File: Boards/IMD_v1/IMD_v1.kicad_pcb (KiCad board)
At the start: 2 copper layers, 25 x 50 mm, 29 parts, among them J1 MM_F_RA_04, J2 UF_2_RA, K1 G5Q-1A4-DC5-5V, Q1 SSM3K333R, Q2 SSM3K333R, U1 Ultrafit_5(IMD), U2 TLV3701QDBVRG4Q1, U3 TLV3701QDBVRG4Q1, U4 CD4044BPWR

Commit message: Layout after check in with Corey
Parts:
- C1: footprint Formula:C_0805_OEM -> footprints:C_0805_OEM
- C2: footprint Formula:C_1206_OEM -> footprints:C_1206_OEM
- D1: footprint Formula:DO-214AA -> footprints:DO-214AA
- D2, D4: footprint Formula:LED_0805_OEM -> footprints:LED_0805_OEM
- D3: footprint Formula:D_0805_OEM -> footprints:D_0805_OEM
- F1: footprint Formula:Fuse_1210 -> footprints:Fuse_1210
- J1: footprint Formula:micromatch_female_ra_4 -> footprints:micromatch_female_ra_4
- J2: value UF_2_RA -> UF_2_VT; footprint Formula:Ultrafit_2_RA -> footprints:Ultrafit_2
- K1: footprint Formula:Relay_SPST_OMRON-G5Q-1A4_OEM -> footprints:Relay_SPST_OMRON-G5Q-1A4_OEM
- Q1, Q2: footprint Formula:SOT-23F -> footprints:SOT-23F
- R1, R10, R11, R12, R13, R2, R3, R4, R5, R6, R7, R8, R9: footprint Formula:R_0805_OEM -> footprints:R_0805_OEM
- U1: footprint Formula:Ultrafit_5 -> footprints:Ultrafit_5
- U2, U3: footprint Formula:SOT-23-5_OEM -> footprints:SOT-23-5_OEM
- U4: footprint Formula:TSSOP-16-OEM -> footprints:TSSOP-16-OEM
- moved J1 9.98 mm to (95.5, 89.2)
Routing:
- net +12V: track 11.0 -> 25.5 mm, vias 0 -> 2
- net GND: track 55.8 -> 68.7 mm, vias 6 -> 10
- net /IMD_Status_Output: track 63.6 -> 72.9 mm
- net /12V_Fused: track 90.6 -> 96.6 mm, vias 5 -> 6
- net (no net): track 5.06 -> 0.18 mm
- net Net-(D3-Pad2): track 33.8 -> 36.6 mm
- net Net-(J2-Pad2): track 17.5 -> 18.7 mm
- net Net-(D4-Pad1): track 23.6 -> 24.4 mm, vias 1 -> 0
- removed copper zone on F.Cu, net GND
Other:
- board text added: "GREEN = GOOD"
- board text removed: "LED ON = IMD GOOD"

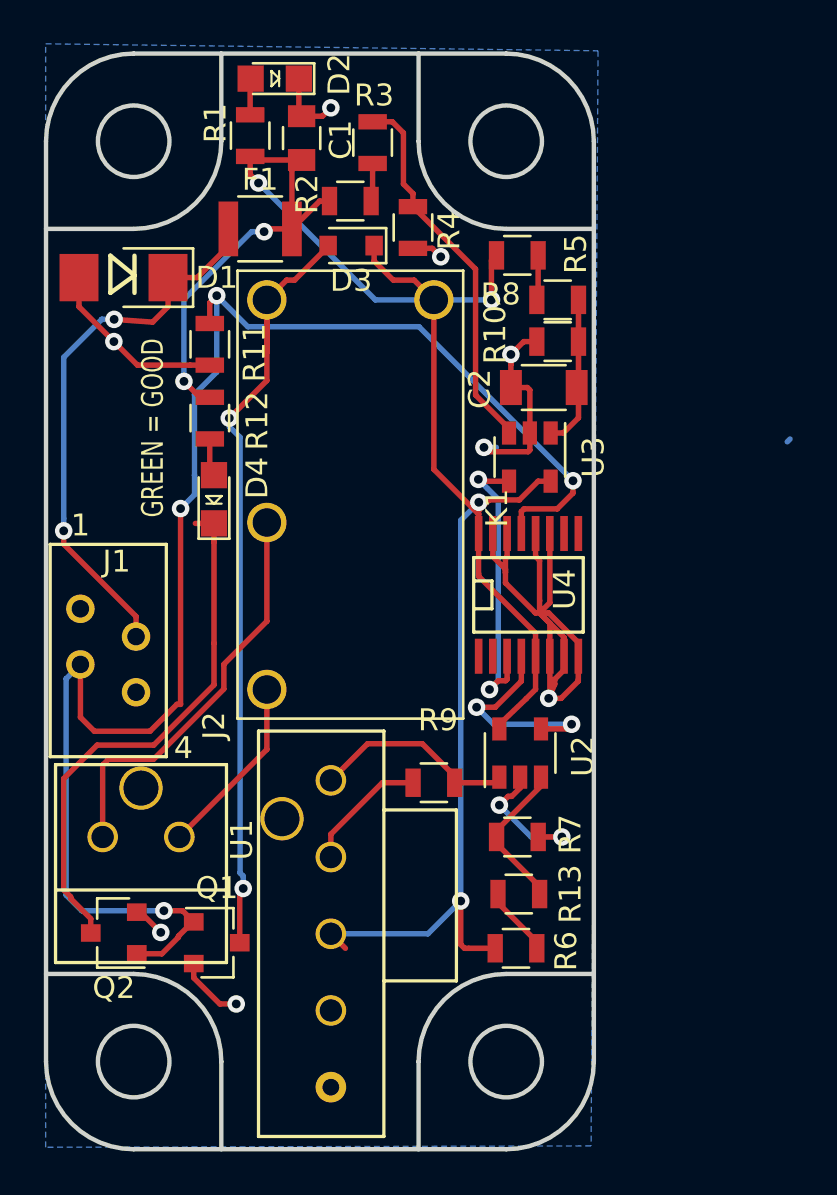
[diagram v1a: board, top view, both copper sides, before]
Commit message: Layout try 3, much less GND islands, and better silkscreen
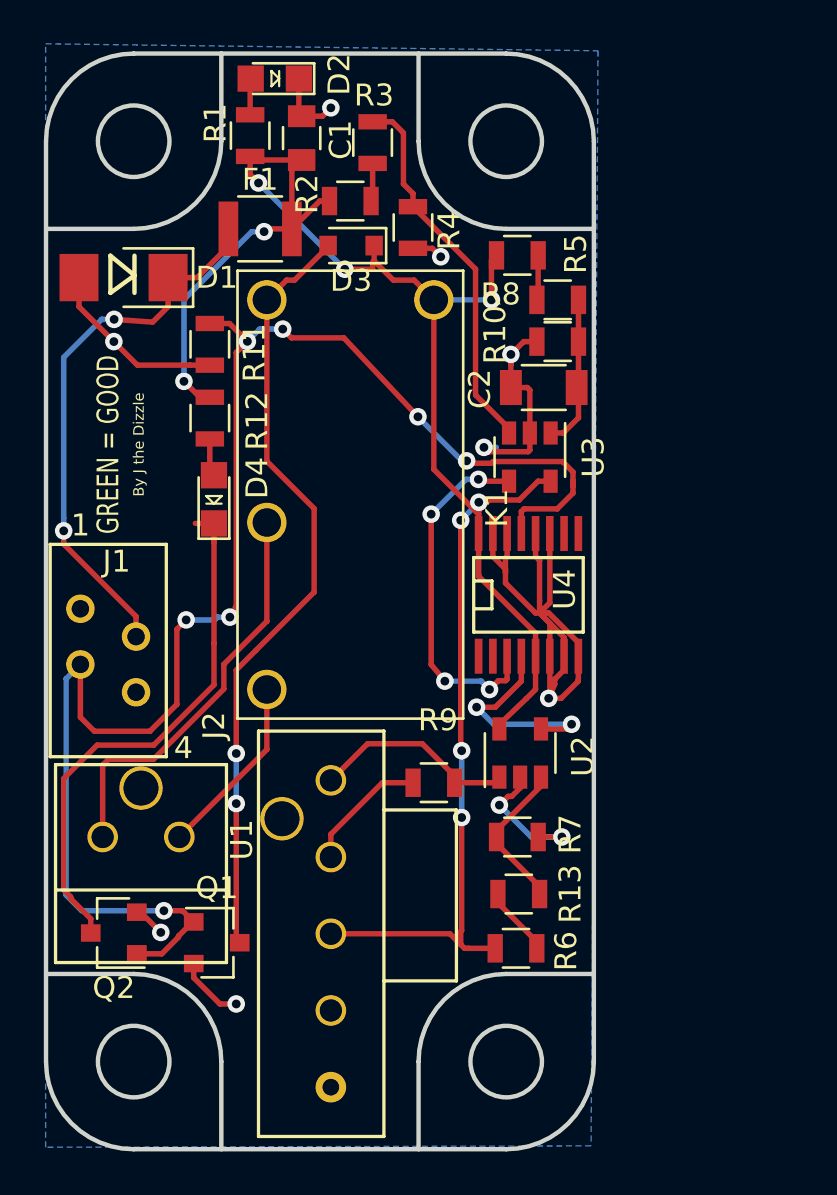
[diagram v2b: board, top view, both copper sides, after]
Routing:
- net /12V_Fused: track 96.6 -> 92.0 mm, vias 6 -> 9
- net Net-(U3-Pad4): track 13.6 -> 16.5 mm, vias 2 -> 4
- net Net-(D3-Pad2): track 36.6 -> 35.6 mm
- net /IMD_Status_Output: track 72.9 -> 72.8 mm, vias 4 -> 7
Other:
- net class formula added: clearance 0.1524, trace_width 0.1524, via_dia 0.6096, via_drill 0.3048
- rule trace_min: 0.2 -> 0.1524
- board text added: "By J the Dizzle"

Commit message: IMD Latch Comparator Fix
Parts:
- turned U2 to 270 degrees
- turned U3 to 90 degrees
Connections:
- U2 pad 3: Net-(R13-Pad2) -> /imd_side_out
- U2 pad 4: Net-(U2-Pad4) -> Net-(R13-Pad2)
- U3 pad 1: Net-(C2-Pad1) -> /delay_side_out
- U3 pad 3: Net-(R3-Pad2) -> Net-(C2-Pad1)
- U3 pad 4: Net-(U3-Pad4) -> Net-(R3-Pad2)
- U4 pad 3: Net-(U3-Pad4) -> /delay_side_out
- U4 pad 4: Net-(U2-Pad4) -> /imd_side_out
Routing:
- net Net-(U3-Pad4): track 16.5 -> 0.00 mm, vias 4 -> 0
- net /delay_side_out: track 0.00 -> 16.5 mm, vias 0 -> 4
- net Net-(U2-Pad4): track 9.81 -> 0.00 mm, vias 2 -> 0
- net Net-(R9-Pad1): track 9.40 -> 16.4 mm, vias 0 -> 2
- net /IMD_Status_Output: track 72.8 -> 68.4 mm
- net /imd_side_out: track 0.00 -> 3.94 mm
- net Net-(R3-Pad2): track 17.3 -> 20.1 mm, vias 0 -> 2
- net GND: track 68.7 -> 66.1 mm, vias 10 -> 8
- net Net-(C2-Pad1): track 6.94 -> 8.80 mm
- net /12V_Fused: track 92.0 -> 93.0 mm
- net Net-(R13-Pad2): track 6.99 -> 6.02 mm
- net Net-(J2-Pad2): track 18.7 -> 19.6 mm
- net Net-(D4-Pad1): vias 0 -> 2
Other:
- outline, holes or cut-outs redrawn
- net class Default: clearance 0.2 -> 0.1524; trace_width 0.25 -> 0.1524; via_dia 0.8 -> 0.6096; via_drill 0.4 -> 0.3048
- net class formula removed
- rule trace_clearance: 0.2 -> 0.1524
- rule via_min_drill: 0.3 -> 0.3048
- rule via_min_size: 0.4 -> 0.6096
- board text added: "IMD LATCH Jamie Santiago"
- board text removed: "By J the Dizzle"

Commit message: IMD update
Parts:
- J2: value UF_2_VT -> mm_2; footprint footprints:Ultrafit_2 -> footprints:mm_2
- moved J2 1.91 mm to (98.4, 94.5), turned to 180 degrees
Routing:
- net Net-(J2-Pad2): track 19.6 -> 15.5 mm
- net Net-(J2-Pad1): track 8.38 -> 10.6 mm

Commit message: IMD DRC checked
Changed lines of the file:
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@@
     (thickness 1.6)
     (drawings 26)
-    (tracks 338)
+    (tracks 335)
     (zones 0)
     (modules 29)
@@
   )
   (setup
-    (last_trace_width 0.762)
+    (last_trace_width 0.1524)
     (user_trace_width 0.762)
     (trace_clearance 0.1524)
@@
   (segment (start 104.013 84.6455) (end 104.013 80.137) (width 0.762) (layer F.Cu) (net 10))
   (segment (start 101.724598 88.648402) (end 100.05259 90.32041) (width 0.762) (layer F.Cu) (net 10))
-  (segment (start 101.724598 86.933902) (end 101.95759 86.70091) (width 0.762) (layer F.Cu) (net 10))
   (segment (start 101.724598 88.648402) (end 101.724598 86.933902) (width 0.762) (layer F.Cu) (net 10))
-  (segment (start 102.05001 86.60849) (end 101.95759 86.70091) (width 0.762) (layer F.Cu) (net 10))
-  (segment (start 101.95759 86.70091) (end 104.013 84.6455) (width 0.762) (layer F.Cu) (net 10))
   (segment (start 100.05259 91.59041) (end 98.425 93.218) (width 0.762) (layer F.Cu) (net 10))
   (segment (start 100.05259 90.32041) (end 100.05259 91.59041) (width 0.762) (layer F.Cu) (net 10))
+  (segment (start 104.013 84.6455) (end 101.724598 86.933902) (width 0.762) (layer F.Cu) (net 10))
   (segment (start 99.186999 94.996001) (end 98.425 95.758) (width 0.762) (layer F.Cu) (net 11))
   (segment (start 102.152401 92.030599) (end 99.186999 94.996001) (width 0.762) (layer F.Cu) (net 11))
@@
   (segment (start 115.626 86.239) (end 115.626 87.23433) (width 0.25) (layer F.Cu) (net 22))
   (via (at 113.665 78.1685) (size 0.8) (drill 0.4) (layers F.Cu B.Cu) (net 23))
-  (via (at 114.173 87.757) (size 0.8) (drill 0.4) (layers F.Cu B.Cu) (net 23))
-  (segment (start 114.976 87.289) (end 114.907999 87.357001) (width 0.25) (layer F.Cu) (net 23))
-  (segment (start 114.572999 87.357001) (end 114.173 87.757) (width 0.25) (layer F.Cu) (net 23))
-  (segment (start 114.907999 87.357001) (end 114.572999 87.357001) (width 0.25) (layer F.Cu) (net 23))
-  (segment (start 114.976 86.239) (end 114.976 87.289) (width 0.25) (layer F.Cu) (net 23))
   (segment (start 113.099315 78.1685) (end 111.511815 79.756) (width 0.25) (layer B.Cu) (net 23))
   (segment (start 113.665 78.1685) (end 113.099315 78.1685) (width 0.25) (layer B.Cu) (net 23))
   (via (at 111.511815 79.756) (size 0.8) (drill 0.4) (layers F.Cu B.Cu) (net 23))
   (segment (start 111.511815 79.756) (end 111.511815 86.619815) (width 0.25) (layer F.Cu) (net 23))
-  (via (at 112.134826 87.376) (size 0.8) (drill 0.4) (layers F.Cu B.Cu) (net 23))
   (segment (start 112.268 87.376) (end 112.134826 87.376) (width 0.25) (layer F.Cu) (net 23))
   (segment (start 111.511815 86.619815) (end 112.134826 87.376) (width 0.25) (layer F.Cu) (net 23))
-  (segment (start 113.792 87.376) (end 114.173 87.757) (width 0.25) (layer B.Cu) (net 23))
-  (segment (start 112.134826 87.376) (end 113.792 87.376) (width 0.25) (layer B.Cu) (net 23))
   (segment (start 113.749 78.2525) (end 113.665 78.1685) (width 0.1524) (layer F.Cu) (net 23))
   (segment (start 115.0645 78.2525) (end 113.749 78.2525) (width 0.25) (layer F.Cu) (net 23))
+  (segment (start 114.976 87.289) (end 114.641 87.289) (width 0.25) (layer F.Cu) (net 23))
+  (via (at 114.173 87.757) (size 0.8) (drill 0.4) (layers F.Cu B.Cu) (net 23))
+  (segment (start 114.641 87.289) (end 114.173 87.757) (width 0.25) (layer F.Cu) (net 23))
+  (segment (start 112.134826 87.376) (end 113.792 87.376) (width 0.25) (layer B.Cu) (net 23))
+  (segment (start 113.792 87.376) (end 114.173 87.757) (width 0.25) (layer B.Cu) (net 23))
+  (via (at 112.134826 87.376) (size 0.8) (drill 0.4) (layers F.Cu B.Cu) (net 23))
+  (segment (start 114.976 86.239) (end 114.976 87.289) (width 0.25) (layer F.Cu) (net 23))
   (zone (net 2) (net_name GND) (layer B.Cu) (hatch edge 0.508)
     (connect_pads (clearance 0.508))

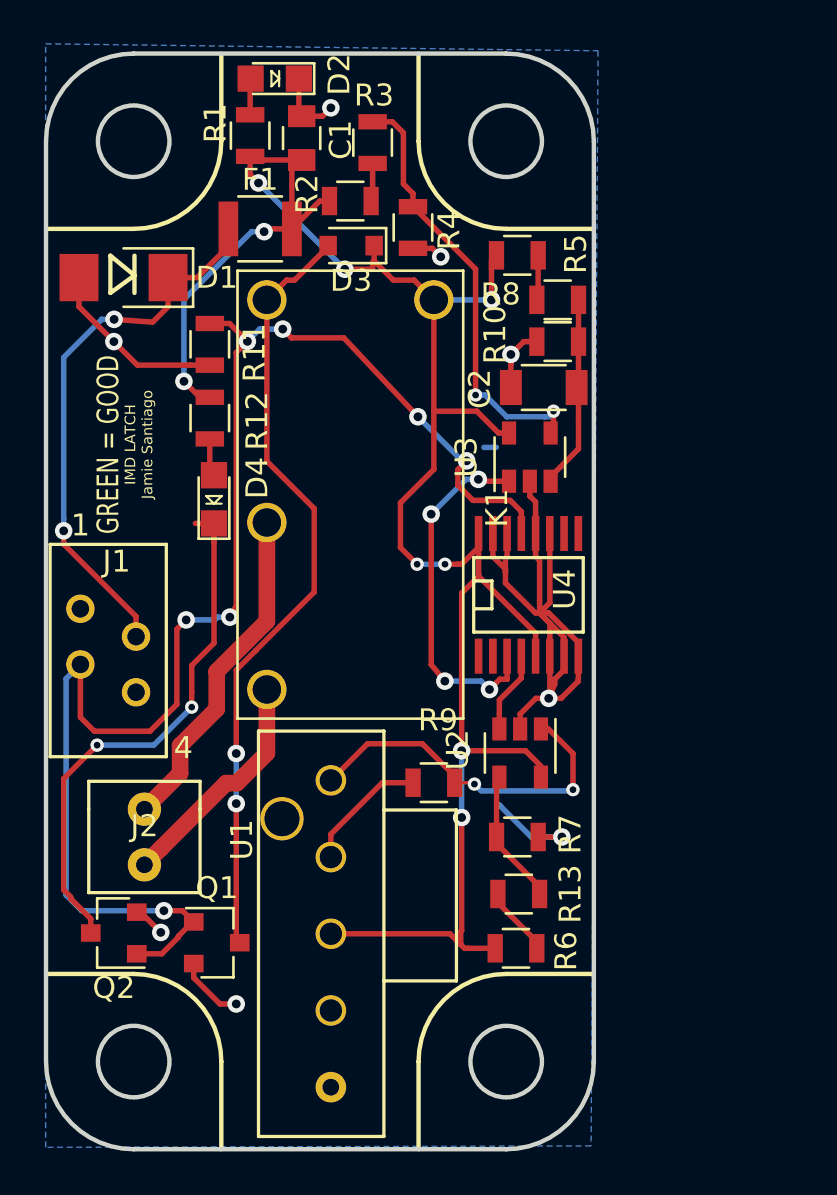
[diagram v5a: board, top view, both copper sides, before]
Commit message: Layout and Schematic with microfit v 2
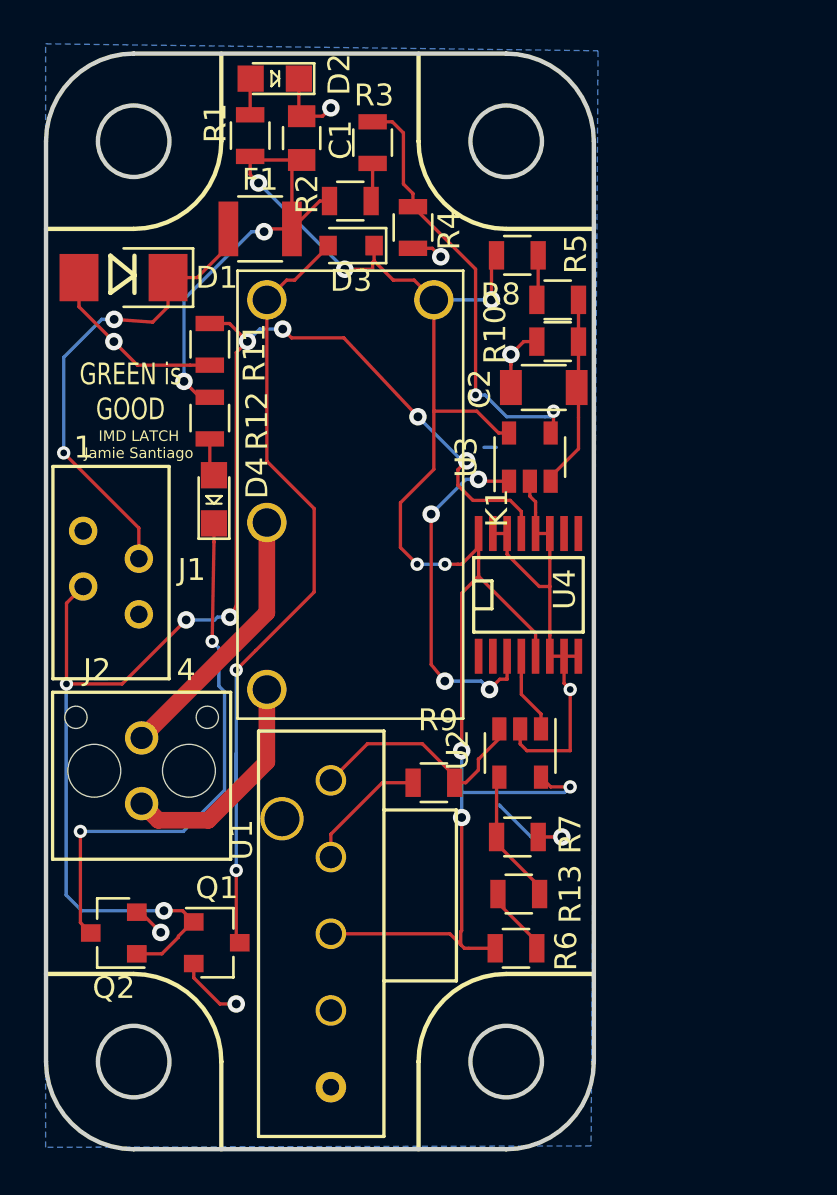
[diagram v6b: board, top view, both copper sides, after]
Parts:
- J2: value mm_2 -> MicroFit_V_2; footprint footprints:mm_2 -> footprints:MicroFit_V_2
- moved J1 3.56 mm to (95.6, 85.6)
- moved J2 1.53 mm to (98.3, 93.0), turned to 0 degrees
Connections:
- U2 pad 1: Net-(R9-Pad1) -> /imd_side_out
- U2 pad 3: /imd_side_out -> Net-(R9-Pad1)
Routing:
- net GND: track 66.1 -> 55.1 mm
- net Net-(R9-Pad1): track 16.4 -> 10.9 mm, vias 2 -> 0
- net +12V: track 25.5 -> 22.1 mm
- net Net-(J2-Pad2): track 15.4 -> 12.2 mm
- net /12V_Fused: track 93.0 -> 95.5 mm, vias 9 -> 10
- net Net-(D3-Pad2): track 35.6 -> 37.9 mm
- net /IMD_Status_Output: track 68.4 -> 67.3 mm, vias 7 -> 8
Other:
- board text added: "GREEN is GOOD"
- board text removed: "GREEN = GOOD"
